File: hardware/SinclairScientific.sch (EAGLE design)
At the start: 33 parts, among them SW1 SPST_TACT-KMR2, U2 SPX3819-3.3, U3 MCP73831T-2ACI/OT, X1 JSTPH, X2 32.768, X3 microUSB

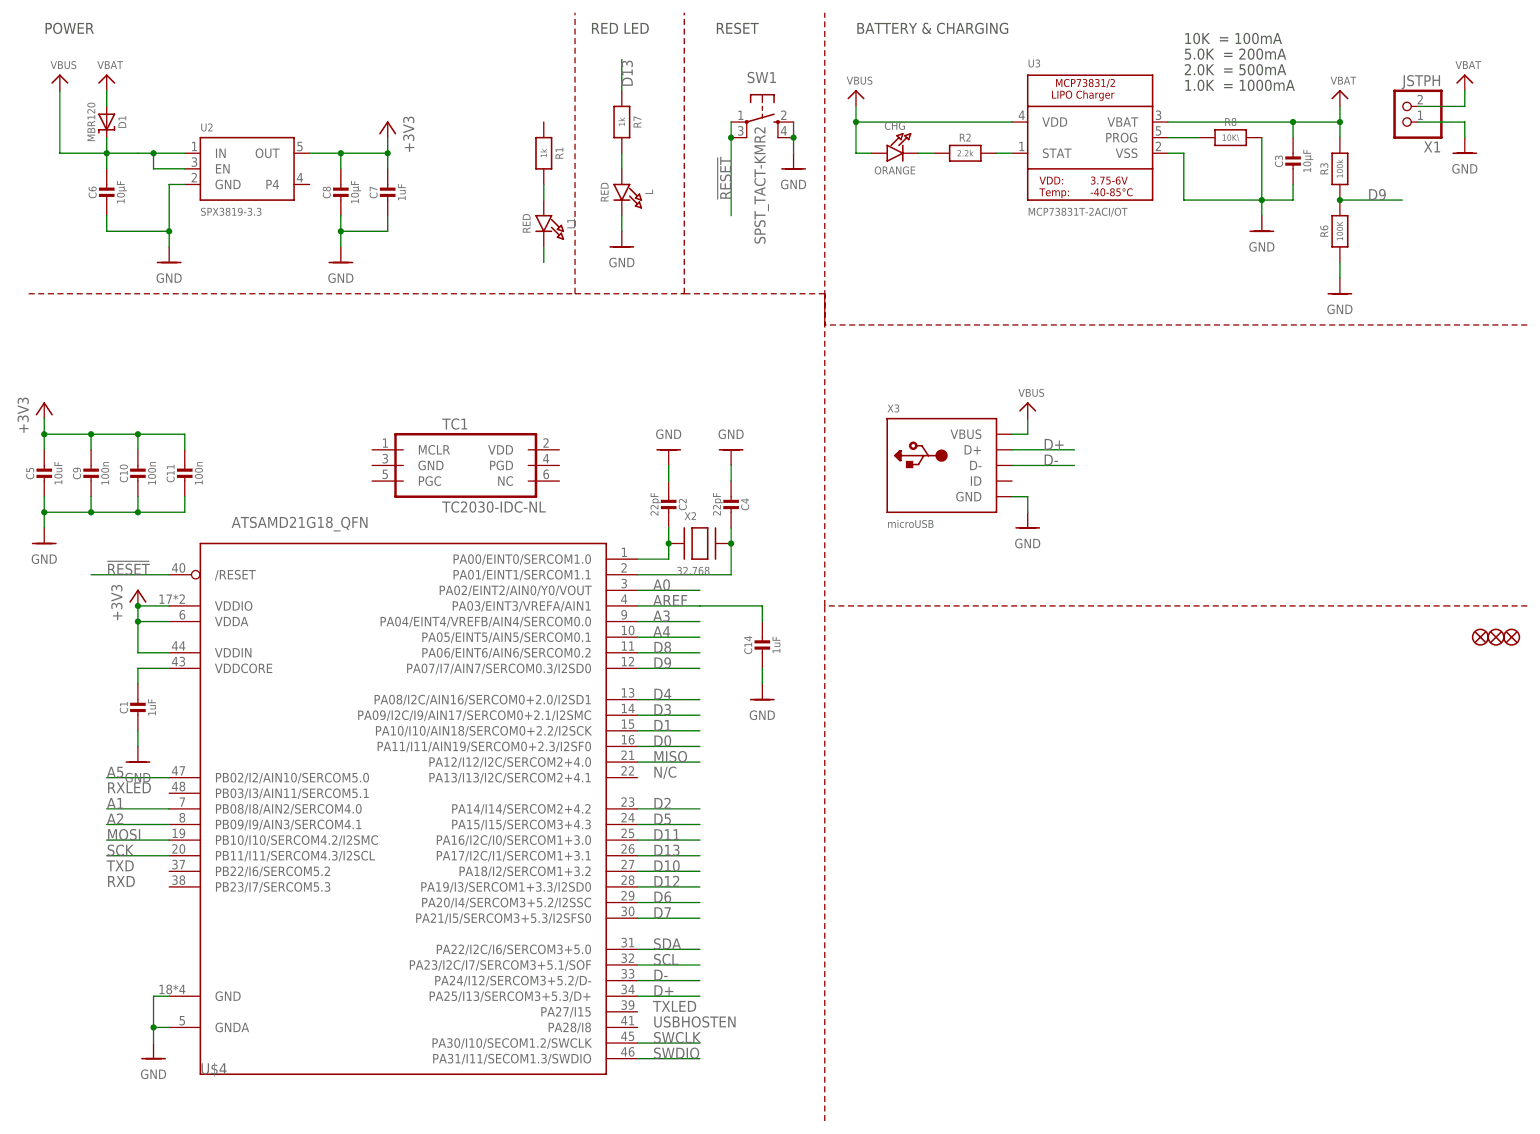
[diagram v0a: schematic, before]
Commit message: Added more to schematic, started PCB placement, still WIP
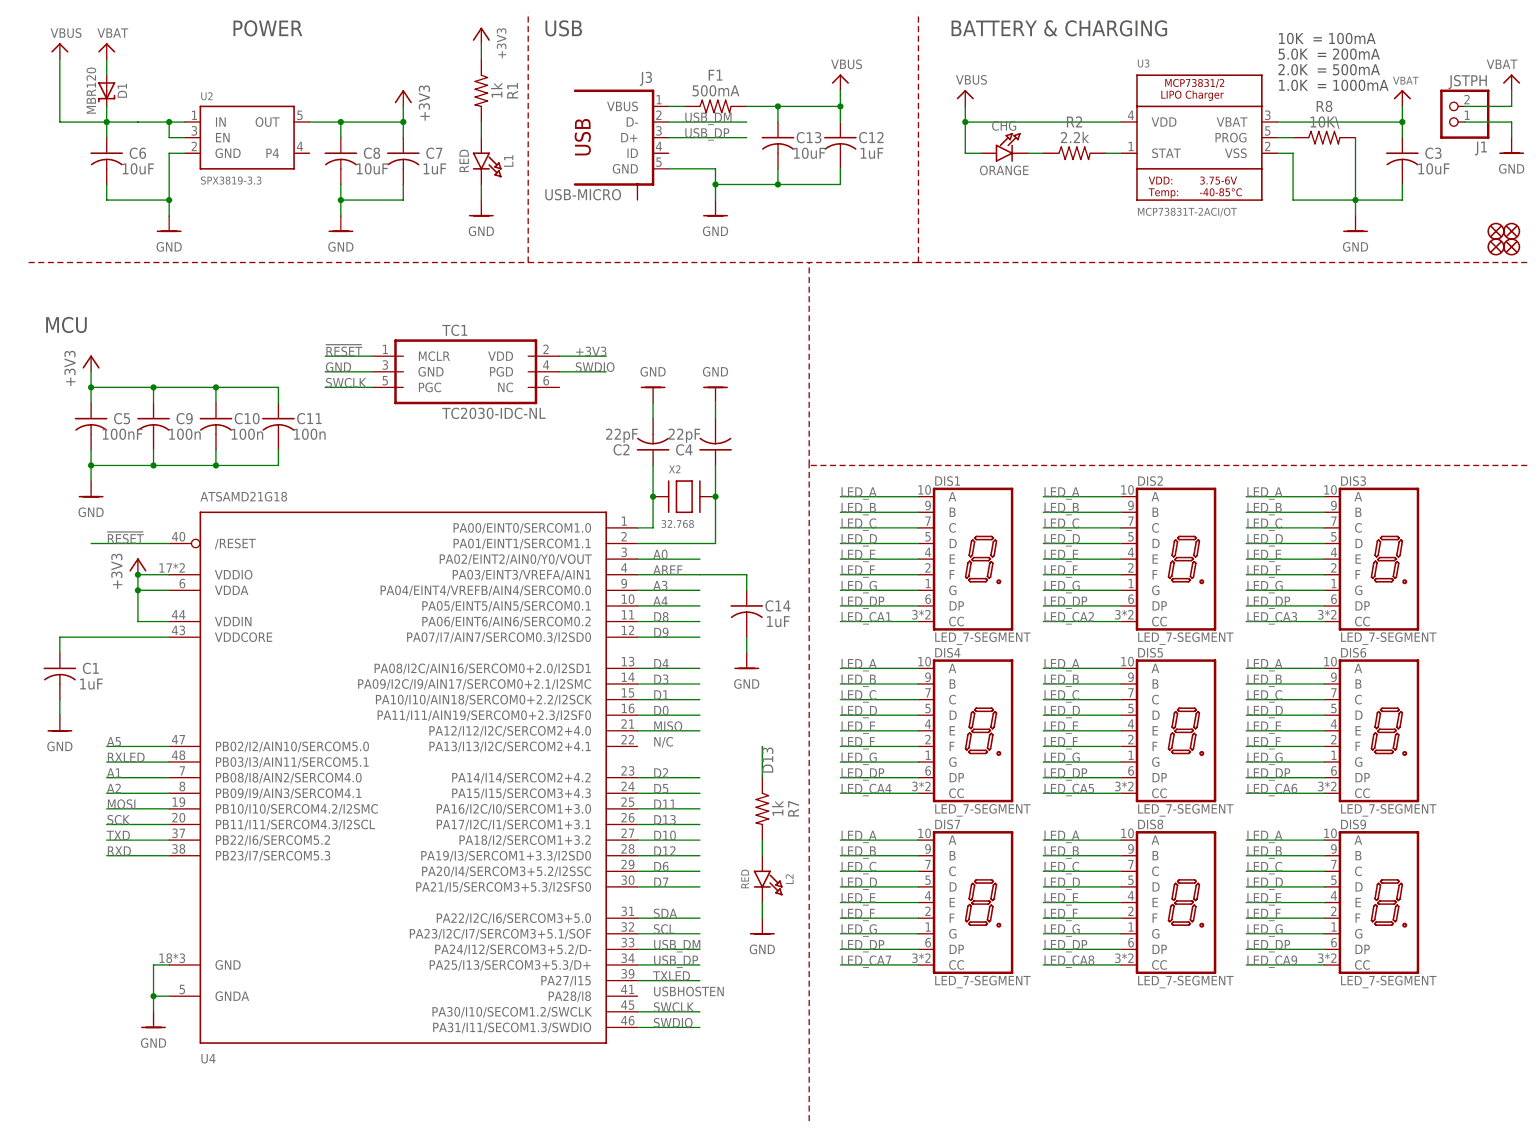
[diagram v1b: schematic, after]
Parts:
- removed L: RED, SinclairScientific:LED0805_NOOUTLINE
- removed R3: 100k, SinclairScientific:RESISTOR_0603_NOOUT
- removed R6: 100K, SinclairScientific:RESISTOR_0603_NOOUT
- removed SW1: SPST_TACT-KMR2, SinclairScientific:SPST_TACT-KMR2
- removed U$4: ATSAMD21G18_QFN, SinclairScientific:ATSAMD21J_QFN
- removed X1: JSTPH, SinclairScientific:CON_JST_PH_2PIN
- removed X3: microUSB, SinclairScientific:USB_MICRO_20329_V2
- added C12: 1uF, gametroller:C-USC0603
- added C13: 10uF, gametroller:C-USC0805
- added DIS1, DIS2, DIS3, DIS4, DIS5, DIS6, DIS7, DIS8, DIS9: LED_7-SEGMENT, SinclairScientific:LED_7-SEGMENT
- added F1: 500mA, gametroller:R-US_R0805
- added J1: JSTPH, SinclairScientific:CON_JST_PH_2PIN
- added J3: USB-MICRO, gametroller:USB-MICRO
- added L2: RED, SinclairScientific:LED0805_NOOUTLINE
- added U$2: FIDUCIAL"", SinclairScientific:FIDUCIAL""
- added U4: ATSAMD21G18, gametroller:ATSAMD21J_QFP
- C1, C10, C11, C14, C2, C4, C7, C9: device SinclairScientific:CAP_CERAMIC0603_NO -> gametroller:C-USC0603
- C3, C6, C8: value 10µF -> 10uF; device SinclairScientific:CAP_CERAMIC0805-NOOUTLINE -> gametroller:C-USC0805
- C5: value 10uF -> 100nF; device SinclairScientific:CAP_CERAMIC0805-NOOUTLINE -> gametroller:C-USC0603
- R1, R2, R7, R8: device SinclairScientific:RESISTOR_0603_NOOUT -> gametroller:R-US_R0603
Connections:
- removed net D+: U$4.PA25/I13/SERCOM3+5.3/D+, X3.D+
- removed net D-: U$4.PA24/I12/SERCOM3+5.2/D-, X3.D-
- removed net GND1: L1.C
- new net LED_A: DIS1.A, DIS2.A, DIS3.A, DIS4.A, DIS5.A, DIS6.A, DIS7.A, DIS8.A, DIS9.A
- new net LED_B: DIS1.B, DIS2.B, DIS3.B, DIS4.B, DIS5.B, DIS6.B, DIS7.B, DIS8.B, DIS9.B
- new net LED_C: DIS1.C, DIS2.C, DIS3.C, DIS4.C, DIS5.C, DIS6.C, DIS7.C, DIS8.C, DIS9.C
- new net LED_CA1: DIS1.CC
- new net LED_CA2: DIS2.CC
- new net LED_CA3: DIS3.CC
- new net LED_CA4: DIS4.CC
- new net LED_CA5: DIS5.CC
- new net LED_CA6: DIS6.CC
- new net LED_CA7: DIS7.CC
- new net LED_CA8: DIS8.CC
- new net LED_CA9: DIS9.CC
- new net LED_D: DIS1.D, DIS2.D, DIS3.D, DIS4.D, DIS5.D, DIS6.D, DIS7.D, DIS8.D, DIS9.D
- new net LED_DP: DIS1.DP, DIS2.DP, DIS3.DP, DIS4.DP, DIS5.DP, DIS6.DP, DIS7.DP, DIS8.DP, DIS9.DP
- new net LED_E: DIS1.E, DIS2.E, DIS3.E, DIS4.E, DIS5.E, DIS6.E, DIS7.E, DIS8.E, DIS9.E
- new net LED_F: DIS1.F, DIS2.F, DIS3.F, DIS4.F, DIS5.F, DIS6.F, DIS7.F, DIS8.F, DIS9.F
- new net LED_G: DIS1.G, DIS2.G, DIS3.G, DIS4.G, DIS5.G, DIS6.G, DIS7.G, DIS8.G, DIS9.G
- new net N$8: F1.1, J3.VBUS
- new net RXD: U4.PB23/I7/SERCOM5.3
- new net RXLED: U4.PB03/I3/AIN11/SERCOM5.1
- new net TXD: U4.PB22/I6/SERCOM5.2
- new net TXLED: U4.PA27/I15
- new net USB_DM: J3.D-, U4.PA24/I12/SERCOM3+5.2/D-
- new net USB_DP: J3.D+, U4.PA25/I13/SERCOM3+5.3/D+
- net !RESET: now also TC1.MCLR, U4./RESET; no longer SW1.P, SW1.P1, U$4./RESET
- net +3V3: now also R1.1, TC1.VDD, U4.VDDA, U4.VDDIN, U4.VDDIO; no longer U$4.VDDA, U$4.VDDIN, U$4.VDDIO
- net A0: now also U4.PA02/EINT2/AIN0/Y0/VOUT; no longer U$4.PA02/EINT2/AIN0/Y0/VOUT
- net A1: now also U4.PB08/I8/AIN2/SERCOM4.0; no longer U$4.PB08/I8/AIN2/SERCOM4.0
- net A2: now also U4.PB09/I9/AIN3/SERCOM4.1; no longer U$4.PB09/I9/AIN3/SERCOM4.1
- net A3: now also U4.PA04/EINT4/VREFB/AIN4/SERCOM0.0; no longer U$4.PA04/EINT4/VREFB/AIN4/SERCOM0.0
- net A4: now also U4.PA05/EINT5/AIN5/SERCOM0.1; no longer U$4.PA05/EINT5/AIN5/SERCOM0.1
- net A5: now also U4.PB02/I2/AIN10/SERCOM5.0; no longer U$4.PB02/I2/AIN10/SERCOM5.0
- net AREF: now also U4.PA03/EINT3/VREFA/AIN1; no longer U$4.PA03/EINT3/VREFA/AIN1
- net D0: now also U4.PA11/I11/AIN19/SERCOM0+2.3/I2SF0; no longer U$4.PA11/I11/AIN19/SERCOM0+2.3/I2SF0
- net D1: now also U4.PA10/I10/AIN18/SERCOM0+2.2/I2SCK; no longer U$4.PA10/I10/AIN18/SERCOM0+2.2/I2SCK
- net D10: now also U4.PA18/I2/SERCOM1+3.2; no longer U$4.PA18/I2/SERCOM1+3.2
- net D11: now also U4.PA16/I2C/I0/SERCOM1+3.0; no longer U$4.PA16/I2C/I0/SERCOM1+3.0
- net D12: now also U4.PA19/I3/SERCOM1+3.3/I2SD0; no longer U$4.PA19/I3/SERCOM1+3.3/I2SD0
- net D13: now also U4.PA17/I2C/I1/SERCOM1+3.1; no longer U$4.PA17/I2C/I1/SERCOM1+3.1
- net D2: now also U4.PA14/I14/SERCOM2+4.2; no longer U$4.PA14/I14/SERCOM2+4.2
- net D3: now also U4.PA09/I2C/I9/AIN17/SERCOM0+2.1/I2SMC; no longer U$4.PA09/I2C/I9/AIN17/SERCOM0+2.1/I2SMC
- net D4: now also U4.PA08/I2C/AIN16/SERCOM0+2.0/I2SD1; no longer U$4.PA08/I2C/AIN16/SERCOM0+2.0/I2SD1
- net D5: now also U4.PA15/I15/SERCOM3+4.3; no longer U$4.PA15/I15/SERCOM3+4.3
- net D6: now also U4.PA20/I4/SERCOM3+5.2/I2SSC; no longer U$4.PA20/I4/SERCOM3+5.2/I2SSC
- net D7: now also U4.PA21/I5/SERCOM3+5.3/I2SFS0; no longer U$4.PA21/I5/SERCOM3+5.3/I2SFS0
- net D8: now also U4.PA06/EINT6/AIN6/SERCOM0.2; no longer U$4.PA06/EINT6/AIN6/SERCOM0.2
- net D9: now also U4.PA07/I7/AIN7/SERCOM0.3/I2SD0; no longer R3.2, R6.1, U$4.PA07/I7/AIN7/SERCOM0.3/I2SD0
- net GND: now also C12.2, C13.2, J1.1, J3.GND, L1.C, L2.C, TC1.GND, U4.GND, U4.GNDA; no longer L.C, R6.2, SW1.S, SW1.S1, U$4.GND, U$4.GNDA, X1.1, X3.GND
- net MISO: now also U4.PA12/I12/I2C/SERCOM2+4.0; no longer U$4.PA12/I12/I2C/SERCOM2+4.0
- net MOSI: now also U4.PB10/I10/SERCOM4.2/I2SMC; no longer U$4.PB10/I10/SERCOM4.2/I2SMC
- net N$2: now also L2.A; no longer L.A
- net N$5: now also U4.PA00/EINT0/SERCOM1.0; no longer U$4.PA00/EINT0/SERCOM1.0
- net N$7: now also U4.PA01/EINT1/SERCOM1.1; no longer U$4.PA01/EINT1/SERCOM1.1
- net SCK: now also U4.PB11/I11/SERCOM4.3/I2SCL; no longer U$4.PB11/I11/SERCOM4.3/I2SCL
- net SCL: now also U4.PA23/I2C/I7/SERCOM3+5.1/SOF; no longer U$4.PA23/I2C/I7/SERCOM3+5.1/SOF
- net SDA: now also U4.PA22/I2C/I6/SERCOM3+5.0; no longer U$4.PA22/I2C/I6/SERCOM3+5.0
- net SWCLK: now also TC1.PGC, U4.PA30/I10/SECOM1.2/SWCLK; no longer U$4.PA30/I10/SECOM1.2/SWCLK
- net SWDIO: now also TC1.PGD, U4.PA31/I11/SECOM1.3/SWDIO; no longer U$4.PA31/I11/SECOM1.3/SWDIO
- net VBAT: now also J1.2; no longer R3.1, X1.2
- net VBUS: now also C12.1, C13.1, F1.2; no longer X3.VBUS
- net VDDCORE: now also U4.VDDCORE; no longer U$4.VDDCORE
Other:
- note added: "MCU"
- note added: "USB"
- note removed: "RED LED"
- note removed: "RESET"
- note removed: "RXD"
- note removed: "RXLED"
- note removed: "TXD"
- note removed: "TXLED"
- moved on the sheet: C1, C10, C11, C14, C2, C3, C4, C5, C6, C7, C8, C9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

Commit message: Schematic nearly finalized, still working on board dimensions and component placement
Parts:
- removed DIS1, DIS2, DIS3, DIS4, DIS5, DIS6, DIS7, DIS8, DIS9: LED_7-SEGMENT, SinclairScientific:LED_7-SEGMENT
- removed L2: RED, SinclairScientific:LED0805_NOOUTLINE
- added C15: 100nF, SinclairScientific:C-USC0603
- added DIS-13, DIS-46, DIS-79: LED_3X7-SEGMENT, SinclairScientific:LED_3X7-SEGMENT
- added HB: RED, SinclairScientific:LED0805_NOOUTLINE
- added R10, R11, R12, R13, R14, R5, R6, R9: 150, SinclairScientific:R-US_R0603
- added R15, R16, R17, R18, R19, R20, R21, R22, R23: 1k, SinclairScientific:R-US_R0603
- added R3, R4: 3.3k, SinclairScientific:R-US_R0603
- added SW-0, SW-1, SW-2, SW-3, SW-4, SW-5, SW-6, SW-7, SW-8, SW-9, SW-C, SW-DIV, SW-DWN, SW-E, SW-MINUS, SW-MULT, SW-PLUS, SW-UP: SPST_TACT-6X6, SinclairScientific:SPST_TACT-6X6
- added T1, T10, T11, T12, T13, T14, T15, T16, T17, T2, T3, T4, T5, T6, T7, T8, T9: (no value), SinclairScientific:NMOSSOT23
- added U5: W25Q128JVSO, SinclairScientific:W25Q128JVSO
- C1, C10, C11, C12, C14, C2, C4, C5, C7, C9: device gametroller:C-USC0603 -> SinclairScientific:C-USC0603
- C13, C3, C6, C8: device gametroller:C-USC0805 -> SinclairScientific:C-USC0805
- CHG: value ORANGE -> RED
- F1: device gametroller:R-US_R0805 -> SinclairScientific:R-US_R0805
- J3: device gametroller:USB-MICRO -> SinclairScientific:USB-MICRO
- R1, R2, R7, R8: device gametroller:R-US_R0603 -> SinclairScientific:R-US_R0603
- U4: device gametroller:ATSAMD21J_QFP -> SinclairScientific:ATSAMD21J_QFP
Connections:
- net RXD renamed D31
- net RXLED renamed D25/RXLED
- net SCL renamed D21/SCL
- net SDA renamed D20/SDA
- net TXD renamed D30
- net TXLED renamed D26/TXLED
- removed net A0: U4.PA02/EINT2/AIN0/Y0/VOUT
- removed net A1: U4.PB08/I8/AIN2/SERCOM4.0
- removed net A2: U4.PB09/I9/AIN3/SERCOM4.1
- removed net A3: U4.PA04/EINT4/VREFB/AIN4/SERCOM0.0
- removed net A4: U4.PA05/EINT5/AIN5/SERCOM0.1
- removed net A5: U4.PB02/I2/AIN10/SERCOM5.0
- removed net D8: U4.PA06/EINT6/AIN6/SERCOM0.2
- removed net D9: U4.PA07/I7/AIN7/SERCOM0.3/I2SD0
- removed net MISO: U4.PA12/I12/I2C/SERCOM2+4.0
- removed net MOSI: U4.PB10/I10/SERCOM4.2/I2SMC
- removed net SCK: U4.PB11/I11/SERCOM4.3/I2SCL
- new net D14/A0: T7.G, U4.PA02/EINT2/AIN0/Y0/VOUT
- new net D15/A1: SW-2.S, SW-2.S1, SW-DWN.S, SW-DWN.S1, T15.G, U4.PB08/I8/AIN2/SERCOM4.0
- new net D16/A2: SW-8.S, SW-8.S1, SW-E.S, SW-E.S1, T13.G, U4.PB09/I9/AIN3/SERCOM4.1
- new net D17/A3: SW-7.S, SW-7.S1, SW-UP.S, SW-UP.S1, T12.G, U4.PA04/EINT4/VREFB/AIN4/SERCOM0.0
- new net D18/A4: T8.G, U4.PA05/EINT5/AIN5/SERCOM0.1
- new net D19/A5: T4.G, U4.PB02/I2/AIN10/SERCOM5.0
- new net D22/MISO: U4.PA12/I12/I2C/SERCOM2+4.0, U5.DO/IO1
- new net D23/MOSI: U4.PB10/I10/SERCOM4.2/I2SMC, U5.DI/IO0
- new net D24/SCK: U4.PB11/I11/SERCOM4.3/I2SCL, U5.CLK
- new net D27: U4.PA28/I8
- new net D39: U4.PA13/I13/I2C/SERCOM2+4.1, U5.!CS
- new net D8/A6: R4.1, SW-0.P, SW-0.P1, SW-C.P, SW-C.P1, SW-DIV.P, SW-DIV.P1, SW-DWN.P, SW-DWN.P1, SW-E.P, SW-E.P1, SW-MINUS.P, SW-MINUS.P1, SW-MULT.P, SW-MULT.P1, SW-PLUS.P, SW-PLUS.P1, SW-UP.P, SW-UP.P1, T2.G, U4.PA06/EINT6/AIN6/SERCOM0.2
- new net D9/A7: R3.1, SW-1.P, SW-1.P1, SW-2.P, SW-2.P1, SW-3.P, SW-3.P1, SW-4.P, SW-4.P1, SW-5.P, SW-5.P1, SW-6.P, SW-6.P1, SW-7.P, SW-7.P1, SW-8.P, SW-8.P1, SW-9.P, SW-9.P1, T5.G, U4.PA07/I7/AIN7/SERCOM0.3/I2SD0
- new net N$10: R6.2, T2.D
- new net N$11: R9.2, T3.D
- new net N$12: R10.2, T4.D
- new net N$13: R11.2, T5.D
- new net N$14: R12.2, T6.D
- new net N$15: R13.2, T7.D
- new net N$16: R14.2, T8.D
- new net N$9: R5.2, T1.D
- net +3V3: now also C15.1, T10.D, T11.D, T12.D, T13.D, T14.D, T15.D, T16.D, T17.D, T9.D, U5.!HOLD/!IO3, U5.!WP/!IO2, U5.VCC
- net D10: now also T3.G
- net D11: now also SW-3.S, SW-3.S1, SW-PLUS.S, SW-PLUS.S1, T16.G
- net D12: now also SW-4.S, SW-4.S1, SW-MINUS.S, SW-MINUS.S1, T17.G
- net D2: now also SW-1.S, SW-1.S1, SW-C.S, SW-C.S1, T9.G
- net D3: now also SW-5.S, SW-5.S1, SW-DIV.S, SW-DIV.S1, T10.G
- net D4: now also SW-6.S, SW-6.S1, SW-MULT.S, SW-MULT.S1, T11.G
- net D5: now also T1.G
- net D6: now also T6.G
- net D7: now also SW-0.S, SW-0.S1, SW-9.S, SW-9.S1, T14.G
- net GND: now also C15.2, HB.C, R15.2, R16.2, R17.2, R18.2, R19.2, R20.2, R21.2, R22.2, R23.2, R3.2, R4.2, T1.S, T2.S, T3.S, T4.S, T5.S, T6.S, T7.S, T8.S, U5.GND; no longer L2.C
- net LED_A: now also DIS-13.A, DIS-46.A, DIS-79.A, R5.1; no longer DIS1.A, DIS2.A, DIS3.A, DIS4.A, DIS5.A, DIS6.A, DIS7.A, DIS8.A, DIS9.A
- net LED_B: now also DIS-13.B, DIS-46.B, DIS-79.B, R6.1; no longer DIS1.B, DIS2.B, DIS3.B, DIS4.B, DIS5.B, DIS6.B, DIS7.B, DIS8.B, DIS9.B
- net LED_C: now also DIS-13.C, DIS-46.C, DIS-79.C, R9.1; no longer DIS1.C, DIS2.C, DIS3.C, DIS4.C, DIS5.C, DIS6.C, DIS7.C, DIS8.C, DIS9.C
- net LED_CA1: now also DIS-13.CA1, R15.1, T9.S; no longer DIS1.CC
- net LED_CA2: now also DIS-13.CA2, R16.1, T10.S; no longer DIS2.CC
- net LED_CA3: now also DIS-13.CA3, R17.1, T11.S; no longer DIS3.CC
- net LED_CA4: now also DIS-46.CA1, R18.1, T12.S; no longer DIS4.CC
- net LED_CA5: now also DIS-46.CA2, R19.1, T13.S; no longer DIS5.CC
- net LED_CA6: now also DIS-46.CA3, R20.1, T14.S; no longer DIS6.CC
- net LED_CA7: now also DIS-79.CA1, R21.1, T15.S; no longer DIS7.CC
- net LED_CA8: now also DIS-79.CA2, R22.1, T16.S; no longer DIS8.CC
- net LED_CA9: now also DIS-79.CA3, R23.1, T17.S; no longer DIS9.CC
- net LED_D: now also DIS-13.D, DIS-46.D, DIS-79.D, R10.1; no longer DIS1.D, DIS2.D, DIS3.D, DIS4.D, DIS5.D, DIS6.D, DIS7.D, DIS8.D, DIS9.D
- net LED_DP: now also DIS-13.DP, DIS-46.DP, DIS-79.DP, R14.1; no longer DIS1.DP, DIS2.DP, DIS3.DP, DIS4.DP, DIS5.DP, DIS6.DP, DIS7.DP, DIS8.DP, DIS9.DP
- net LED_E: now also DIS-13.E, DIS-46.E, DIS-79.E, R11.1; no longer DIS1.E, DIS2.E, DIS3.E, DIS4.E, DIS5.E, DIS6.E, DIS7.E, DIS8.E, DIS9.E
- net LED_F: now also DIS-13.F, DIS-46.F, DIS-79.F, R12.1; no longer DIS1.F, DIS2.F, DIS3.F, DIS4.F, DIS5.F, DIS6.F, DIS7.F, DIS8.F, DIS9.F
- net LED_G: now also DIS-13.G, DIS-46.G, DIS-79.G, R13.1; no longer DIS1.G, DIS2.G, DIS3.G, DIS4.G, DIS5.G, DIS6.G, DIS7.G, DIS8.G, DIS9.G
- net N$2: now also HB.A; no longer L2.A
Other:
- note added: "DISPLAY DRIVERS"
- note added: "DISPLAYS"
- note added: "MEMORY"
- note removed: "N/C"
- note removed: "USBHOSTEN"
